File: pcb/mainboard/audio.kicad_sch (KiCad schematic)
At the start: 32 parts, among them J701 Conn_01x02, J702 Conn_01x02, J703 AudioJack3_SwitchT, U701 WM8960

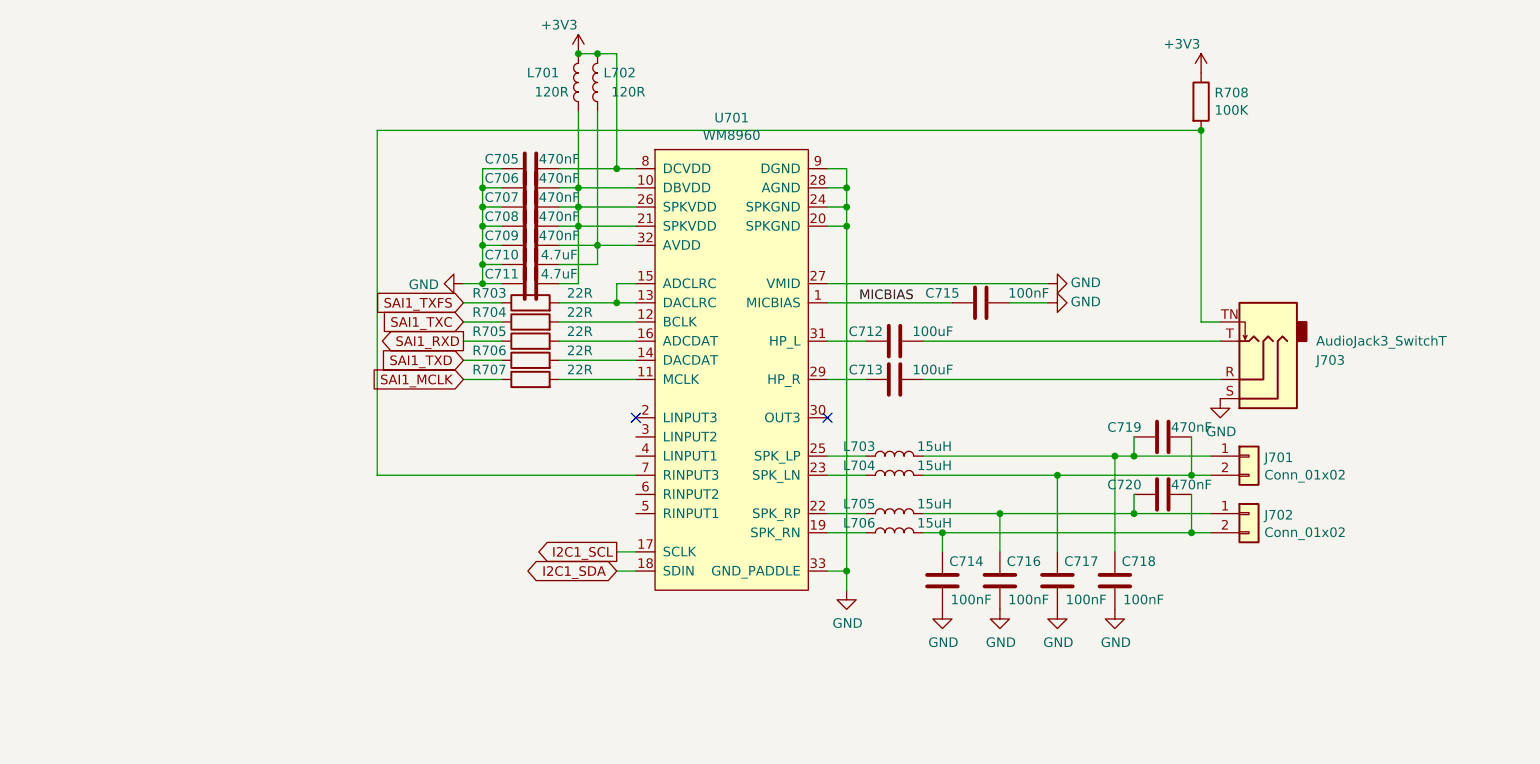
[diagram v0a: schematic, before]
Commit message: pcb: preliminary r0p1 schematics
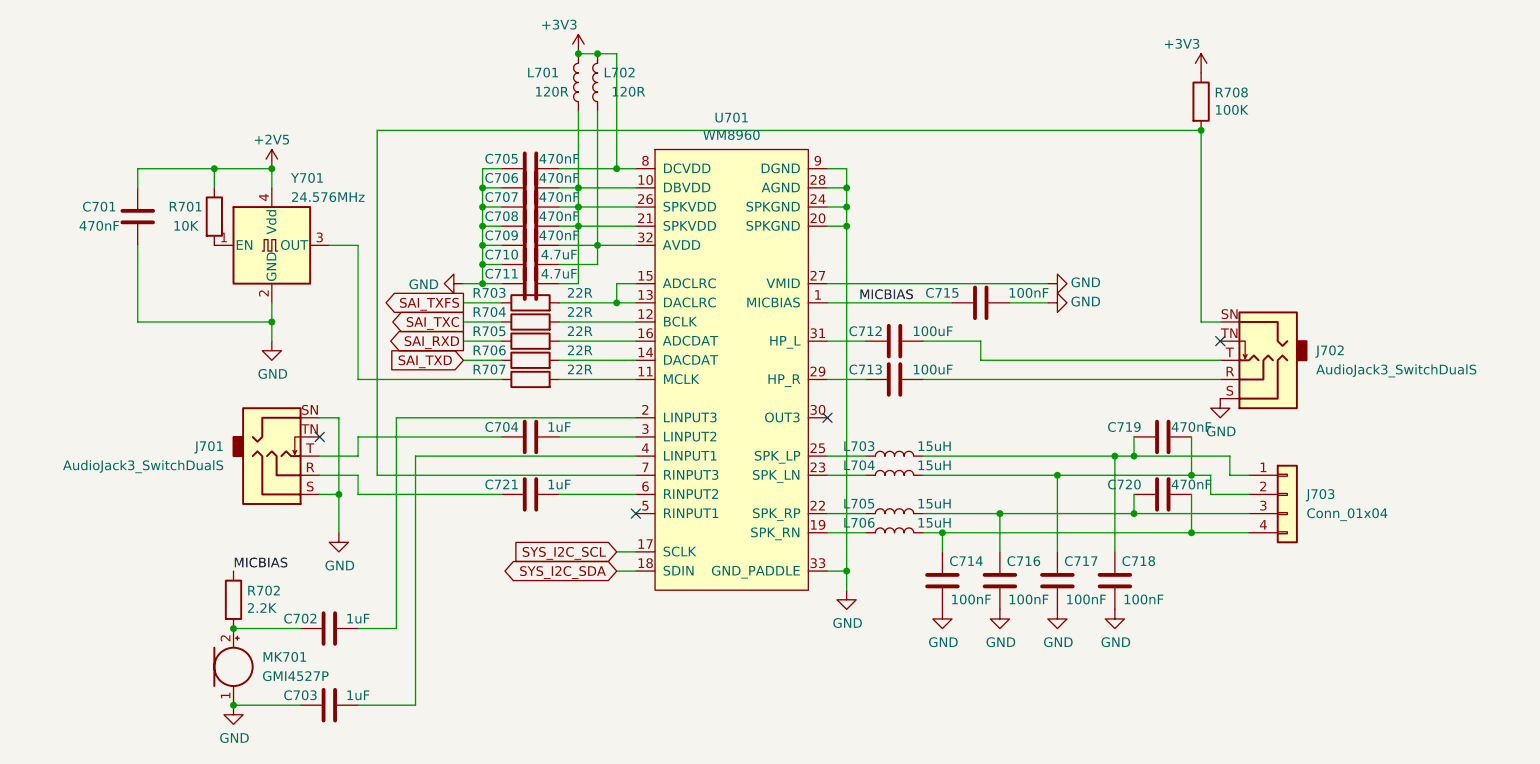
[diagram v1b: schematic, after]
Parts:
- removed J701, J702: Conn_01x02, Connector_PinHeader_2.00mm:PinHeader_1x02_P2.00mm_Vertical, symbol Connector_Generic:Conn_01x02
- removed J703: AudioJack3_SwitchT, footprints:PJ-327E, symbol symbols:AudioJack3_SwitchT
- added C701: 470nF, Capacitor_SMD:C_0402_1005Metric, symbol Device:C
- added C702, C703, C704, C721: 1uF, Capacitor_SMD:C_0603_1608Metric, symbol Device:C
- added J701, J702: AudioJack3_SwitchDualS, symbol symbols:AudioJack3_SwitchDualS
- added J703: Conn_01x04, Connector_Hirose:Hirose_DF13C_CL535-0404-8-51_1x04-1MP_P1.25mm_Vertical, symbol Connector_Generic:Conn_01x04
- added MK701: GMI4527P, footprints:MIC_45, symbol Device:Microphone
- added R701: 10K, Capacitor_SMD:C_0402_1005Metric, symbol Device:R
- added R702: 2.2K, Resistor_SMD:R_0402_1005Metric, symbol Device:R
- added Y701: 24.576MHz, Oscillator:Oscillator_SMD_Abracon_ASE-4Pin_3.2x2.5mm, symbol Oscillator:ASE-xxxMHz
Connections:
- net GND: now also C701.1, C703.2, J701.S, J701.SN, J702.S, MK701.1 (-), Y701.2 (GND)
- net MICBIAS: now also R702.1
- net at C718.2, C719.1, L703.2: now also J703.1 (Pin_1)
- net at C713.2: now also J702.R
- net at C712.2: now also J702.T
- net at R708.2, U701.7 (RINPUT3): now also J702.SN
- net at C717.2, C719.2, L704.2: now also J703.2 (Pin_2)
- net at C716.2, C720.1, L705.2: now also J703.3 (Pin_3)
- net at C714.2, C720.2, L706.2: now also J703.4 (Pin_4)
- net at U701.2 (LINPUT3): now also C702.1
- net at U701.3 (LINPUT2): now also C704.1
- net at U701.4 (LINPUT1): now also C703.1
- net at U701.6 (RINPUT2): now also C721.1
- net I2C1_SCL renamed SYS_I2C_SCL
- net I2C1_SDA renamed SYS_I2C_SDA
- net SAI1_MCLK: no longer names the net of R707.1
- net SAI1_MCLK: now also Y701.3 (OUT)
- net SAI1_RXD renamed SAI_RXD
- net SAI1_TXC renamed SAI_TXC
- net SAI1_TXD renamed SAI_TXD
- net SAI1_TXFS renamed SAI_TXFS
- new net: C721.2, J701.R
- new net: C702.2, MK701.2 (+), R702.2
- new net: C704.2, J701.T
- new net: R701.2, Y701.1 (EN)
- new net +2V5: C701.2, R701.1, Y701.4 (Vdd)
- no-connect marks 2 -> 4
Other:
- company: Copyright EI-2030 2021. / Engineer: Wenting Zhang -> Copyright Modos 2021. / Engineer: Wenting Zhang

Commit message: pcb: initial placement for mb
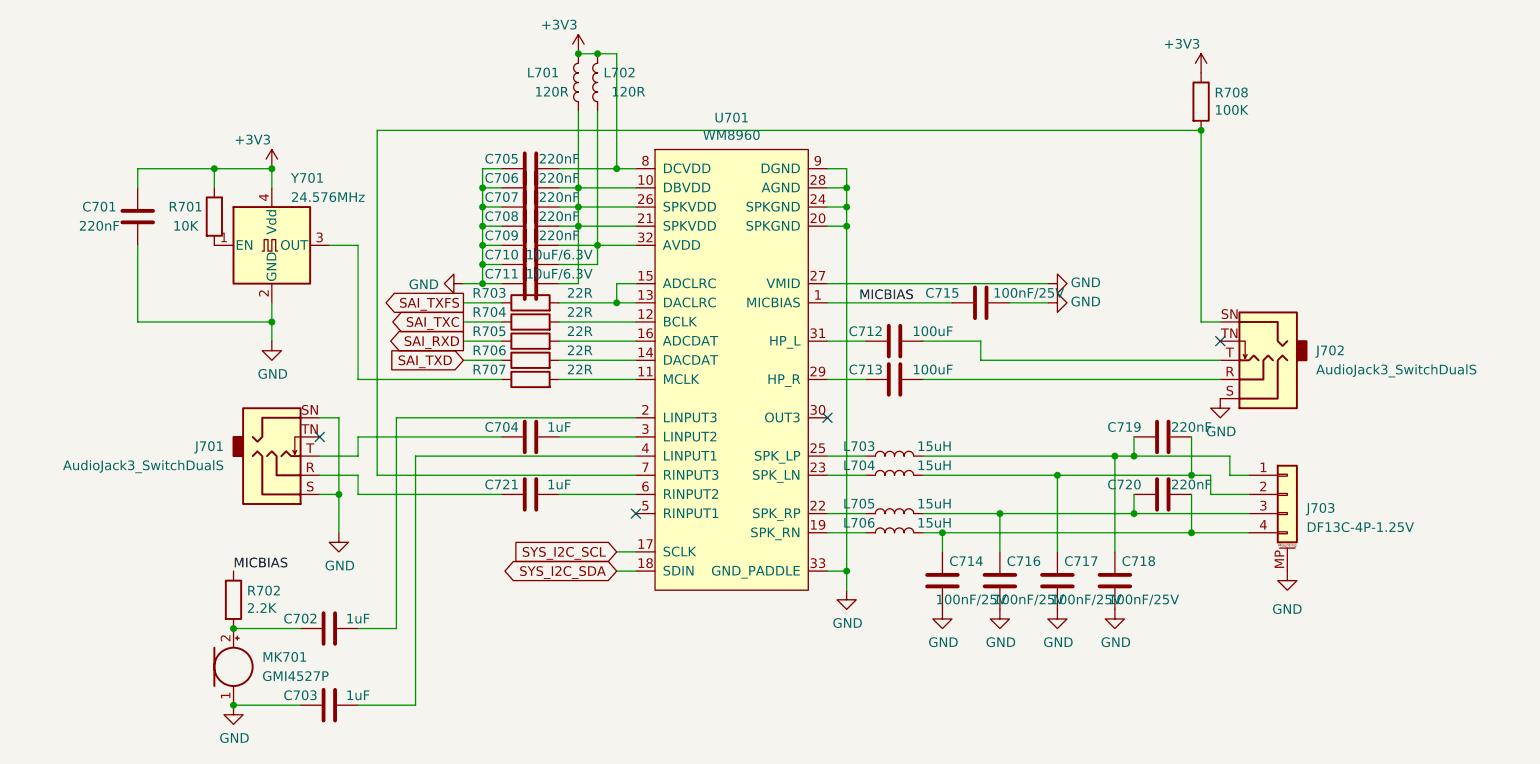
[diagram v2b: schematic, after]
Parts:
- removed J703: Conn_01x04, Connector_Hirose:Hirose_DF13C_CL535-0404-8-51_1x04-1MP_P1.25mm_Vertical, symbol Connector_Generic:Conn_01x04
- added J703: DF13C-4P-1.25V, Connector_Hirose:Hirose_DF13C_CL535-0404-8-51_1x04-1MP_P1.25mm_Vertical, symbol Connector_Generic_MountingPin:Conn_01x04_MountingPin
- C701, C705, C706, C707, C708, C709, C719, C720: value 470nF -> 220nF; LCSC (none) -> C880414; Ref.Price (none) -> 0.0036
- C702, C703, C704, C721: footprint Capacitor_SMD:C_0603_1608Metric -> Capacitor_SMD:C_0402_1005Metric; LCSC (none) -> C157353; Ref.Price (none) -> 0.0034
- C710, C711: value 4.7uF -> 10uF/6.3V; LCSC (none) -> C105490; Ref.Price (none) -> 0.0165
- C712, C713: LCSC (none) -> C178304; Ref.Price (none) -> 0.1211
- C714, C715, C716, C717, C718: value 100nF -> 100nF/25V; LCSC (none) -> C56392; Ref.Price (none) -> 0.0023
- J701, J702: footprint (none) -> footprints:PJ-327E; LCSC (none) -> C145812; Ref.Price (none) -> 0.1229
- L701, L702: LCSC (none) -> C76892; Ref.Price (none) -> 0.0078
- L703, L704, L705, L706: LCSC (none) -> C486329; Ref.Price (none) -> 0.0479
- MK701: LCSC (none) -> C233336; Ref.Price (none) -> 0.2559
- R701: footprint Capacitor_SMD:C_0402_1005Metric -> Resistor_SMD:R_0402_1005Metric; LCSC (none) -> C60489; Ref.Price (none) -> 0.0006
- R702: LCSC (none) -> C163447; Ref.Price (none) -> 0.0007
- R703, R704, R705, R706, R707: LCSC (none) -> C93929; Ref.Price (none) -> 0.002
- R708: LCSC (none) -> C106234; Ref.Price (none) -> 0.0006
- U701: LCSC (none) -> C18752; Ref.Price (none) -> 5.69
- Y701: LCSC (none) -> C387393; Ref.Price (none) -> 0.4166
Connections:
- net +2V5 is gone; now on net +3V3: C701.2, R701.1, Y701.4 (Vdd)
- net GND: now also J703.MP (MountPin)
- net at C718.2, C719.1, L703.2: now also J703.1 (Pin_1)
- net at C717.2, C719.2, L704.2: now also J703.2 (Pin_2)
- net at C716.2, C720.1, L705.2: now also J703.3 (Pin_3)
- net at C714.2, C720.2, L706.2: now also J703.4 (Pin_4)

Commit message: pcb: r0.1 mb routing done
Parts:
- removed J703: DF13C-4P-1.25V, Connector_Hirose:Hirose_DF13C_CL535-0404-8-51_1x04-1MP_P1.25mm_Vertical, symbol Connector_Generic_MountingPin:Conn_01x04_MountingPin
- U701: footprint Package_DFN_QFN:QFN-32-1EP_5x5mm_P0.5mm_EP3.6x3.6mm_ThermalVias -> Package_DFN_QFN:QFN-32-1EP_5x5mm_P0.5mm_EP3.6x3.6mm
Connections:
- net SPK_LP: now reaches C718.2, C719.1, L703.2
- net SPK_LN: now reaches C717.2, C719.2, L704.2
- net SPK_RP: now reaches C716.2, C720.1, L705.2
- net SPK_RN: now reaches C714.2, C720.2, L706.2
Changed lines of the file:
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@@
+    )
+  )
+  (global_label "SPK_LP" (shape output) (at 210.82 119.38 0) (fields_autoplaced)
+    (effects (font (size 1.27 1.27)) (justify left))
+    (property "Intersheet References" "${INTERSHEET_REFS}" (id 0) (at 220.2483 119.3006 0)
+      (effects (font (size 1.27 1.27)) (justify left) hide)
+    )
+  )
+  (global_label "SPK_LN" (shape output) (at 210.82 121.92 0) (fields_autoplaced)
+    (effects (font (size 1.27 1.27)) (justify left))
+    (property "Intersheet References" "${INTERSHEET_REFS}" (id 0) (at 220.3088 121.8406 0)
+      (effects (font (size 1.27 1.27)) (justify left) hide)
+    )
+  )
+  (global_label "SPK_RP" (shape output) (at 210.82 124.46 0) (fields_autoplaced)
+    (effects (font (size 1.27 1.27)) (justify left))
+    (property "Intersheet References" "${INTERSHEET_REFS}" (id 0) (at 220.4902 124.3806 0)
+      (effects (font (size 1.27 1.27)) (justify left) hide)
+    )
+  )
+  (global_label "SPK_RN" (shape output) (at 210.82 127 0) (fields_autoplaced)
+    (effects (font (size 1.27 1.27)) (justify left))
+    (property "Intersheet References" "${INTERSHEET_REFS}" (id 0) (at 220.5507 126.9206 0)
+      (effects (font (size 1.27 1.27)) (justify left) hide)
     )
   )
@@
     )
     (property "Datasheet" "" (id 3) (at 207.01 109.22 0)
-      (effects (font (size 1.27 1.27)) hide)
-    )
-    (pin "1")
-  )
-  (symbol (lib_id "power:GND") (at 215.9 132.08 0) (unit 1)
-    (in_bom yes) (on_board yes) (fields_autoplaced)
-    (property "Reference" "#PWR0113" (id 0) (at 215.9 138.43 0)
-      (effects (font (size 1.27 1.27)) hide)
-    )
-    (property "Value" "GND" (id 1) (at 215.9 137.16 0))
-    (property "Footprint" "" (id 2) (at 215.9 132.08 0)
-      (effects (font (size 1.27 1.27)) hide)
-    )
-    (property "Datasheet" "" (id 3) (at 215.9 132.08 0)
       (effects (font (size 1.27 1.27)) hide)
     )
@@
     (pin "1")
     (pin "2")
-  )
-  (symbol (lib_id "Connector_Generic_MountingPin:Conn_01x04_MountingPin") (at 215.9 121.92 0) (unit 1)
-    (in_bom yes) (on_board yes) (fields_autoplaced)
-    (property "Reference" "J703" (id 0) (at 218.44 123.7614 0)
-      (effects (font (size 1.27 1.27)) (justify left))
-    )
-    (property "Value" "DF13C-4P-1.25V" (id 1) (at 218.44 126.3014 0)
-      (effects (font (size 1.27 1.27)) (justify left))
-    )
-    (property "Footprint" "Connector_Hirose:Hirose_DF13C_CL535-0404-8-51_1x04-1MP_P1.25mm_Vertical" (id 2) (at 215.9 121.92 0)
-      (effects (font (size 1.27 1.27)) hide)
-    )
-    (property "Datasheet" "~" (id 3) (at 215.9 121.92 0)
-      (effects (font (size 1.27 1.27)) hide)
-    )
-    (property "LCSC" "C116890" (id 4) (at 215.9 121.92 0)
-      (effects (font (size 1.27 1.27)) hide)
-    )
-    (property "Ref.Price" "0.1932" (id 5) (at 215.9 121.92 0)
-      (effects (font (size 1.27 1.27)) hide)
-    )
-    (pin "1")
-    (pin "2")
-    (pin "3")
-    (pin "4")
-    (pin "MP")
   )
   (symbol (lib_id "symbols:AudioJack3_SwitchDualS") (at 82.55 121.92 0) (mirror x) (unit 1)
@@
     (property "Reference" "U701" (id 0) (at 142.24 72.009 0))
     (property "Value" "WM8960" (id 1) (at 142.24 74.3204 0))
-    (property "Footprint" "Package_DFN_QFN:QFN-32-1EP_5x5mm_P0.5mm_EP3.6x3.6mm_ThermalVias" (id 2) (at 142.24 73.66 0)
-      (effects (font (size 1.27 1.27)) hide)
-    )
+    (property "Footprint" "Package_DFN_QFN:QFN-32-1EP_5x5mm_P0.5mm_EP3.6x3.6mm" (id 2) (at 142.24 73.66 0)
+      (effects (font (size 1.27 1.27)) hide)
+    )
